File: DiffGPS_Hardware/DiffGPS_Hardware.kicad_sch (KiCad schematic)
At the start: 16 parts, among them U1 Raspberry_Pi, U2 TSR_1-2450, U3 OKI

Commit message: Removed 3.3V OKI
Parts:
- removed C1, C2: 10uF, Capacitor_SMD:C_0603_1608Metric_Pad1.08x0.95mm_HandSolder, symbol Device:C
- removed U3: OKI, MRDT_Devices:OKI_Horizontal, symbol MRDT_Devices:OKI
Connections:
- net +3V3: now also U1.1 (+3V3)
- no-connect marks 48 -> 47
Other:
- moved on the sheet: D3, R3

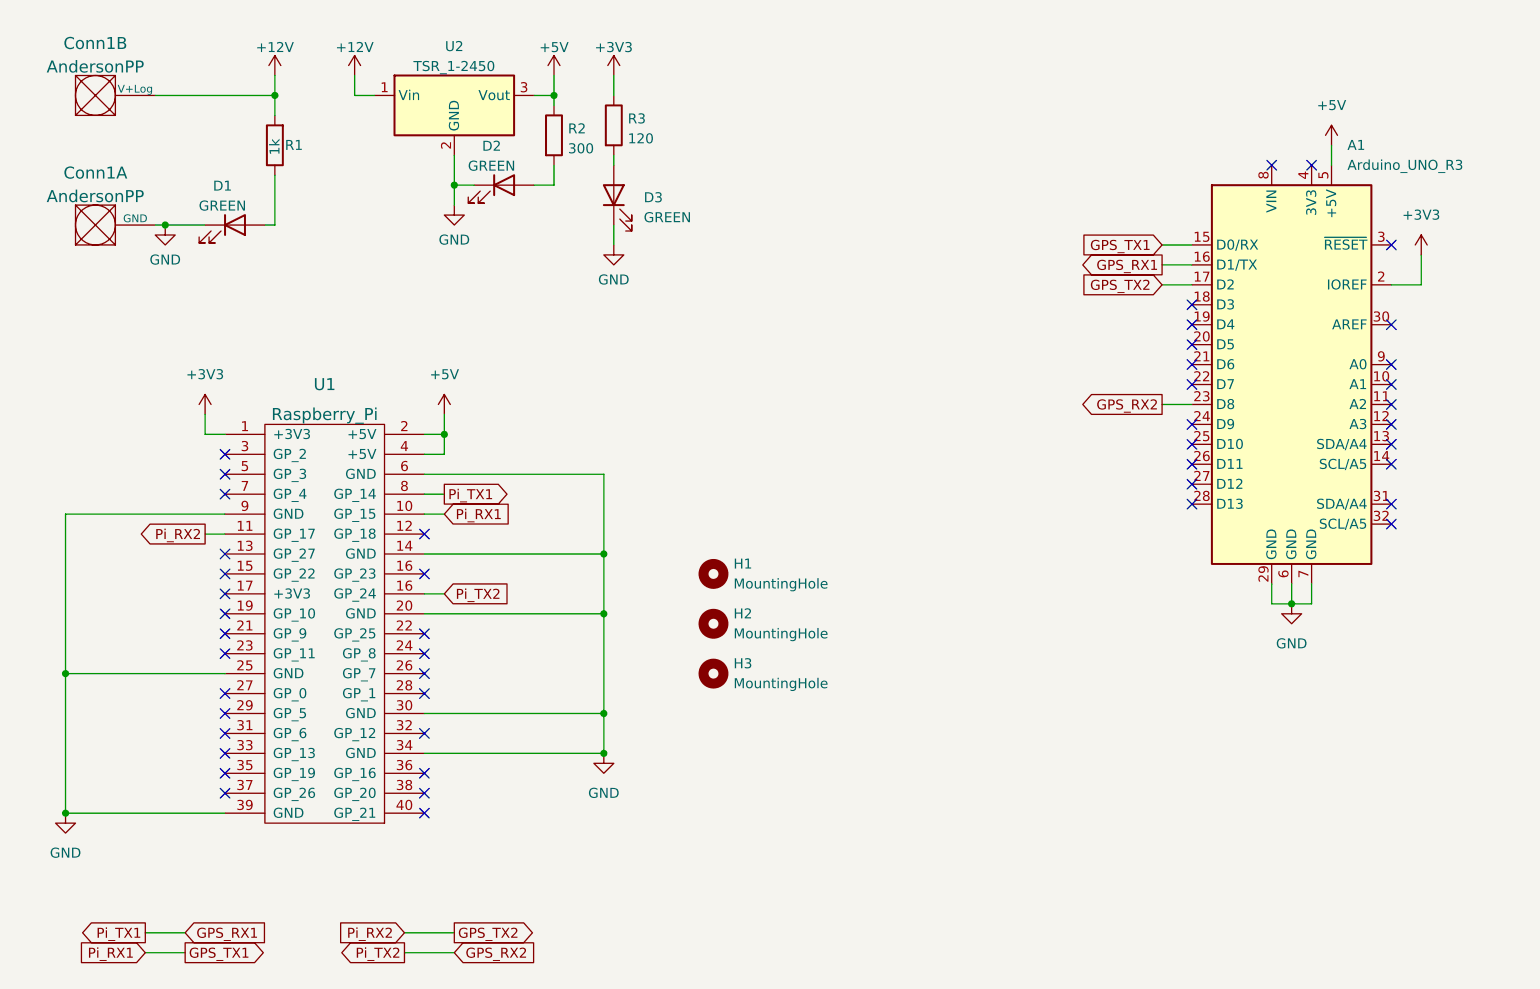
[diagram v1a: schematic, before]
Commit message: Schematic done
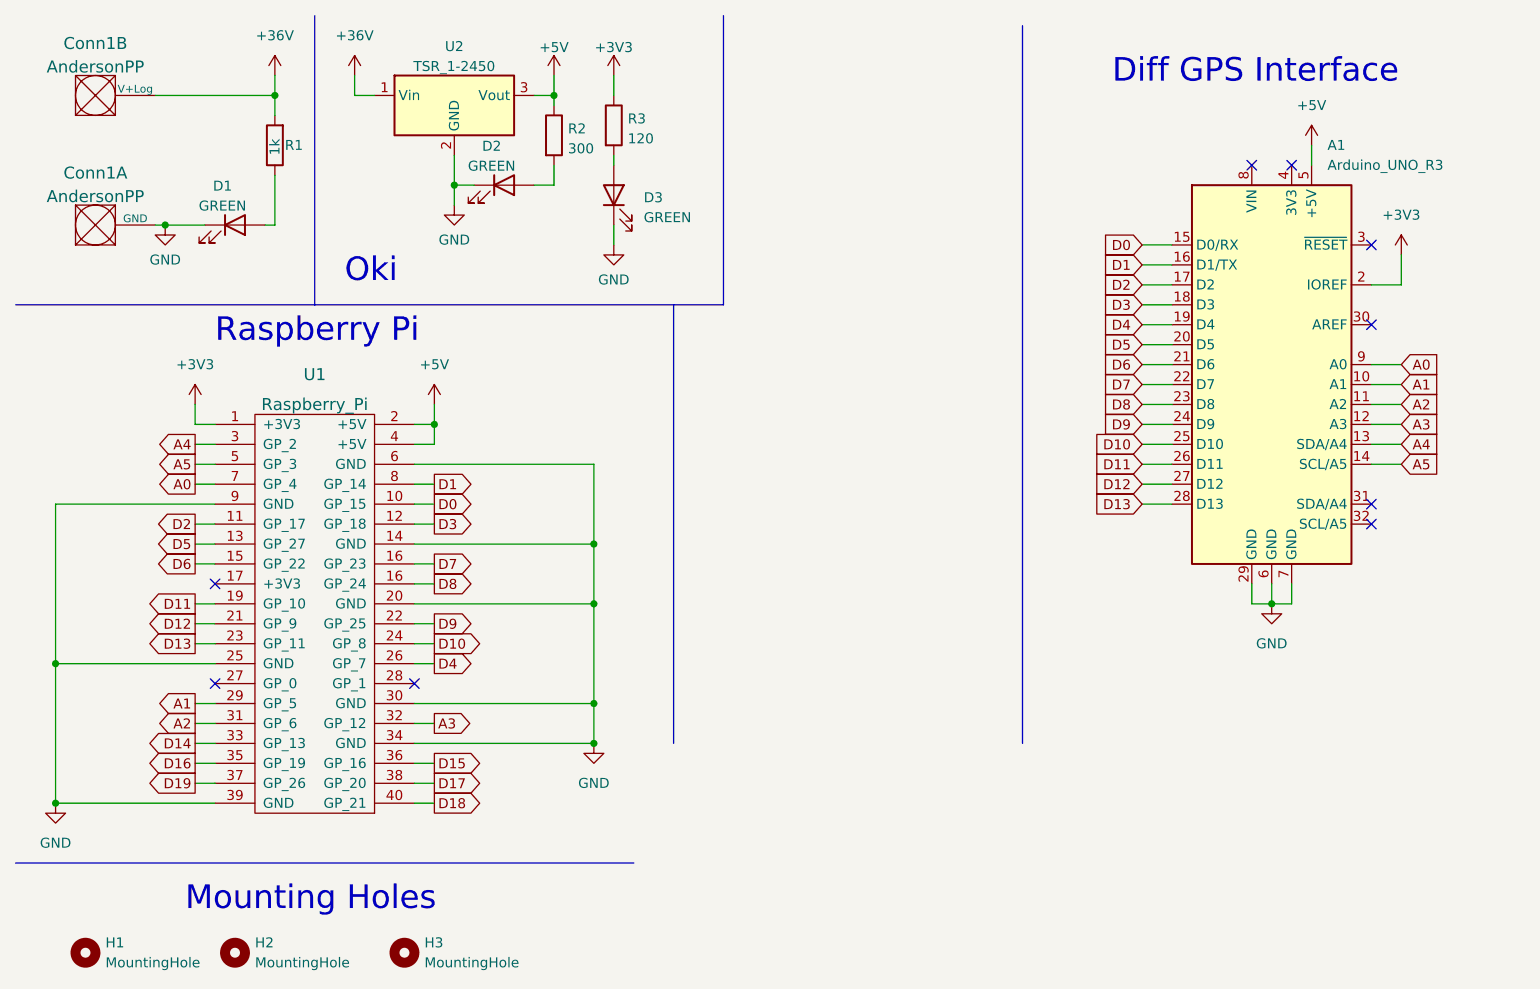
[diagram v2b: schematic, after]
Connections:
- net GPS_RX2 is gone; now on net D8: A1.23 (D8), U1.16 (GP_24)
- net D3: now reaches U1.12 (GP_18)
- net D3: now also A1.18 (D3)
- net D5: now reaches U1.13 (GP_27)
- net D5: now also A1.20 (D5)
- net D6: now reaches U1.15 (GP_22)
- net D6: now also A1.21 (D6)
- net D8: now reaches U1.16 (GP_24)
- net D11: now reaches U1.19 (GP_10)
- net D11: now also A1.26 (D11)
- net D12: now reaches U1.21 (GP_9)
- net D12: now also A1.27 (D12)
- net D9: now reaches U1.22 (GP_25)
- net D9: now also A1.24 (D9)
- net D13: now reaches U1.23 (GP_11)
- net D13: now also A1.28 (D13)
- net D10: now reaches U1.24 (GP_8)
- net D10: now also A1.25 (D10)
- net D4: now reaches U1.26 (GP_7)
- net D4: now also A1.19 (D4)
- net A1: now reaches U1.29 (GP_5)
- net A1: now also A1.10 (A1)
- net A4: now reaches U1.3 (GP_2)
- net A4: now also A1.13 (SDA/A4)
- net A2: now reaches U1.31 (GP_6)
- net A2: now also A1.11 (A2)
- net A3: now reaches U1.32 (GP_12)
- net A3: now also A1.12 (A3)
- net D14: now reaches U1.33 (GP_13)
- net D16: now reaches U1.35 (GP_19)
- net D15: now reaches U1.36 (GP_16)
- net D19: now reaches U1.37 (GP_26)
- net D17: now reaches U1.38 (GP_20)
- net D18: now reaches U1.40 (GP_21)
- net A5: now reaches U1.5 (GP_3)
- net A5: now also A1.14 (SCL/A5)
- net A0: now reaches U1.7 (GP_4)
- net A0: now also A1.9 (A0)
- net D7: now reaches A1.22 (D7)
- net D7: now also U1.16 (GP_24)
- net +12V renamed +36V
- net GPS_RX1 renamed D1
- net GPS_TX1 renamed D0
- net GPS_TX2 renamed D2
- no-connect marks 47 -> 9
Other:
- note added: "Diff GPS Interface"
- note added: "Mounting Holes"
- note added: "Oki"
- note added: "Raspberry Pi"
- moved on the sheet: A1, H1, H2, H3, U1

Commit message: Schematic Review
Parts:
- removed U2: TSR_1-2450, MRDT_Devices:TSR_1-2433, symbol Regulator_Switching:TSR_1-2450
- added C1, C2: 10uF, symbol Device:C
- added H4: MountingHole, MRDT_Drill_Holes:4_40_Hole_Corner, symbol Mechanical:MountingHole
- added U2: OKI, symbol MRDT_Devices:OKI
- R1: value 1k -> 3k
- R3: value 120 -> 100
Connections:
- net +5V: now also C2.2, U2.3 (Vo)
- net GND: now also C1.2, C2.1, U2.2 (GND)
- net +36V renamed VCC
- net VCC: now also Conn1.4 (PV+), C1.1, U2.1 (Vi); no longer Conn1.2 (V+Log)
- net D14: no longer names the net of U1.33 (GP_13)
- net D15: no longer names the net of U1.36 (GP_16)
- net D16: no longer names the net of U1.35 (GP_19)
- net D17: no longer names the net of U1.38 (GP_20)
- net D18: no longer names the net of U1.40 (GP_21)
- net D19: no longer names the net of U1.37 (GP_26)
- no-connect marks 9 -> 15
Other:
- moved on the sheet: D2, D3, R2, R3

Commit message: Finished Layout
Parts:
- C1, C2: footprint (none) -> Capacitor_SMD:C_0603_1608Metric_Pad1.08x0.95mm_HandSolder
- U2: footprint (none) -> MRDT_Devices:OKI_Horizontal
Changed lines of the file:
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@@
       (effects (font (size 1.27 1.27)) (justify right))
     )
-    (property "Footprint" "" (at 81.5848 27.94 0)
+    (property "Footprint" "Capacitor_SMD:C_0603_1608Metric_Pad1.08x0.95mm_HandSolder" (at 81.5848 27.94 0)
       (effects (font (size 1.27 1.27)) hide)
     )
@@
       (effects (font (size 1.27 1.27)) (justify left))
     )
-    (property "Footprint" "" (at 55.5752 35.56 0)
+    (property "Footprint" "Capacitor_SMD:C_0603_1608Metric_Pad1.08x0.95mm_HandSolder" (at 55.5752 35.56 0)
       (effects (font (size 1.27 1.27)) hide)
     )
@@
       (effects (font (size 1.524 1.524)))
     )
-    (property "Footprint" "" (at 59.69 31.75 0)
+    (property "Footprint" "MRDT_Devices:OKI_Horizontal" (at 59.69 31.75 0)
       (effects (font (size 1.524 1.524)) hide)
     )

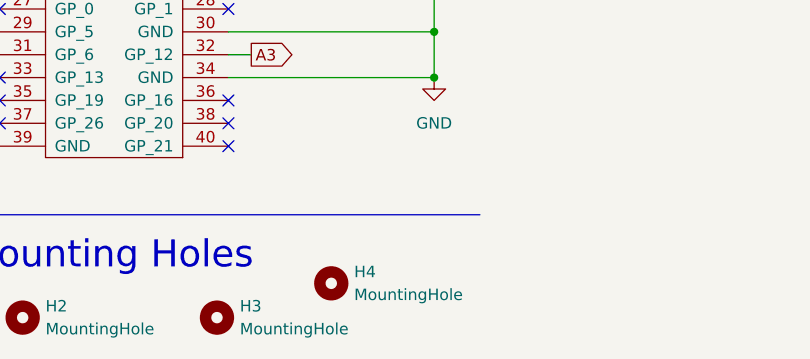
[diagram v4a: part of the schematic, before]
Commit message: Board Review - flipped arduino footprint
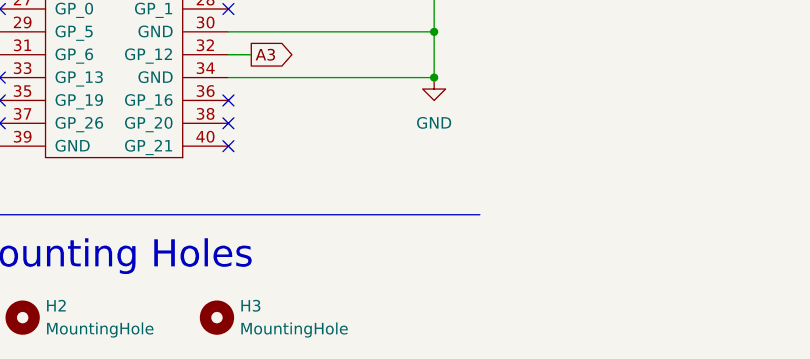
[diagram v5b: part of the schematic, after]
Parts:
- removed H4: MountingHole, MRDT_Drill_Holes:4_40_Hole_Corner, symbol Mechanical:MountingHole
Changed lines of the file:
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@@
-    )
-  )
-  (symbol (lib_id "Mechanical:MountingHole") (at 73.66 127 0) (unit 1)
-    (in_bom yes) (on_board yes) (dnp no) (fields_autoplaced)
-    (property "Reference" "H4" (at 76.2 125.7299 0)
-      (effects (font (size 1.27 1.27)) (justify left))
-    )
-    (property "Value" "MountingHole" (at 76.2 128.2699 0)
-      (effects (font (size 1.27 1.27)) (justify left))
-    )
-    (property "Footprint" "MRDT_Drill_Holes:4_40_Hole_Corner" (at 73.66 127 0)
-      (effects (font (size 1.27 1.27)) hide)
-    )
-    (property "Datasheet" "~" (at 73.66 127 0)
-      (effects (font (size 1.27 1.27)) hide)
-    )
-    (instances
-      (project "DiffGPS_Hardware"
-        (path "/515a2fac-4908-4fa2-9eb8-3ec1d51d96fc"
-          (reference "H4") (unit 1)
-        )
-      )
     )
   )

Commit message: tried to make buck converter
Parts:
- removed U2: OKI, MRDT_Devices:OKI_Horizontal, symbol MRDT_Devices:OKI
- added U2: ~, symbol SHHD003A0A:SHHD003A0A
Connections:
- net +5V: now also U2.4 (Vout+)
- net GND: now also U2.1 (Vin-), U2.6 (Vout-)
- net VCC: now also U2.3 (Vin+)
- no-connect marks 15 -> 16
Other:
- note added: "Buck Converter"
- note removed: "Oki"
- moved on the sheet: C1, C2, D2, D3, R2, R3
